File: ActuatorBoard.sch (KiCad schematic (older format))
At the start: 79 parts, among them J1 Screw_Terminal_01x02, J11 Screw_Terminal_01x02, J12 Screw_Terminal_01x02, J13 Screw_Terminal_01x04, J2 Screw_Terminal_01x02, J3 Screw_Terminal_01x02, J4 Screw_Terminal_01x02, J5 Screw_Terminal_01x02, J7 Screw_Terminal_01x02, J8 Screw_Terminal_01x02, J9 Screw_Terminal_01x02, K1 SANYOU_SRD_Form_B, K2 SANYOU_SRD_Form_B, K3 SANYOU_SRD_Form_B, P1 CONN_01X03, P10 CONN_01X03, P11 CONN_01X03, P12 CONN_01X03, P13 CONN_01X02, P14 SERVO_+, P15 SERVO_-, P16 CONN_01X03, P17 CONN_01X05, P18 CONN_01X08, P19 CONN_01X05, P2 CAN_Conn, P20 CONN_01X08, P21 STEPPER_VCC, P22 CONN_01X05, P23 CONN_01X04, P3 CONN_01X03, P4 CONN_01X03, P5 CONN_01X03, P7 CONN_01X03, P8 CONN_01X03, Q1 BS170, Q2 BS170, Q3 BS170, Q5 IRLR024, U1 MCP2551-I-SN, U2 AT90CAN128-16AU, U3 ULN2003, U4 L7805, Y1 Crystal, Y2 Crystal

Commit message: Added output files
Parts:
- added P6: CONN_01X06, Pin_Headers:Pin_Header_Straight_1x06, symbol CONN_01X06
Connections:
- net +5V: now also P6.1 (P1); no longer P22.1 (P1), P22.2 (P2), P22.3 (P3), P22.4 (P4), P22.5 (P5)
- net +5VD: now also P22.1 (P1), P22.2 (P2), P22.3 (P3), P22.4 (P4), P22.5 (P5)
- net DIRECTION: now also U2.10 ((~SS~)PB0); no longer U2.11 ((SCK)PB1)
- net GND: now also P6.6 (P6)
- net MINI_M2: now also U2.45 ((AD6)PA6); no longer U2.47 ((AD4)PA4)
- net MINI_M3: now also U2.44 ((AD7)PA7); no longer U2.46 ((AD5)PA5)
- net R1: now also U3.3 (I3), U3.4 (I4); no longer U3.1 (I1), U3.2 (I2)
- net R1_SIG: now also U3.13 (O4), U3.14 (O3); no longer U3.15 (O2), U3.16 (O1)
- net R2: now also U3.1 (I1), U3.2 (I2); no longer U3.3 (I3), U3.4 (I4)
- net R2_SIG: now also U3.15 (O2), U3.16 (O1); no longer U3.13 (O4), U3.14 (O3)
- net RX0: now also S1.4, P6.2 (P2); no longer S1.3
- net STEP: now also U2.11 ((SCK)PB1), P6.4 (P4); no longer U2.10 ((~SS~)PB0)
- net TX0: now also S1.3, P6.3 (P3); no longer S1.4
- net RESET: now reaches U2.20 (~RESET)
- net RESET: now also P6.5 (P5)
- net D2: now reaches R11.2
- net D2: now also U2.46 ((AD5)PA5); no longer U2.44 ((AD7)PA7)
- net D1: now reaches R12.2
- net D1: now also U2.47 ((AD4)PA4); no longer U2.45 ((AD6)PA6)
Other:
- moved on the sheet: D13, D14, R11, R12

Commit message: Changed the schematic to look more fancy (pdf update)
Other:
- note added: "3x MOSFET"
- note added: "3x Relay"
- note added: "ADC"
- note added: "AX connections & rx/tx switching"
- note added: "CAN pinout (MCP2551)"
- note added: "Darlington relay driver"
- note added: "Debug LED"
- note added: "Indicator for input\n"
- note added: "Input 12V with diode protection\n"
- note added: "Input 5V with mosfet protection\n\n"
- note added: "Output for I2C\n"
- note added: "PORTB pinout"
- note added: "PORTC pinout"
- note added: "Pinout for kinez servos"
- note added: "Programator pinout"
- note added: "Regulator for 5V logic\n"
- note added: "Stepper driver pinout (A4988)"
- moved on the sheet: A1, C1, C10, C2, C3, C4, C7, C8, C9, D10, D13, D14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

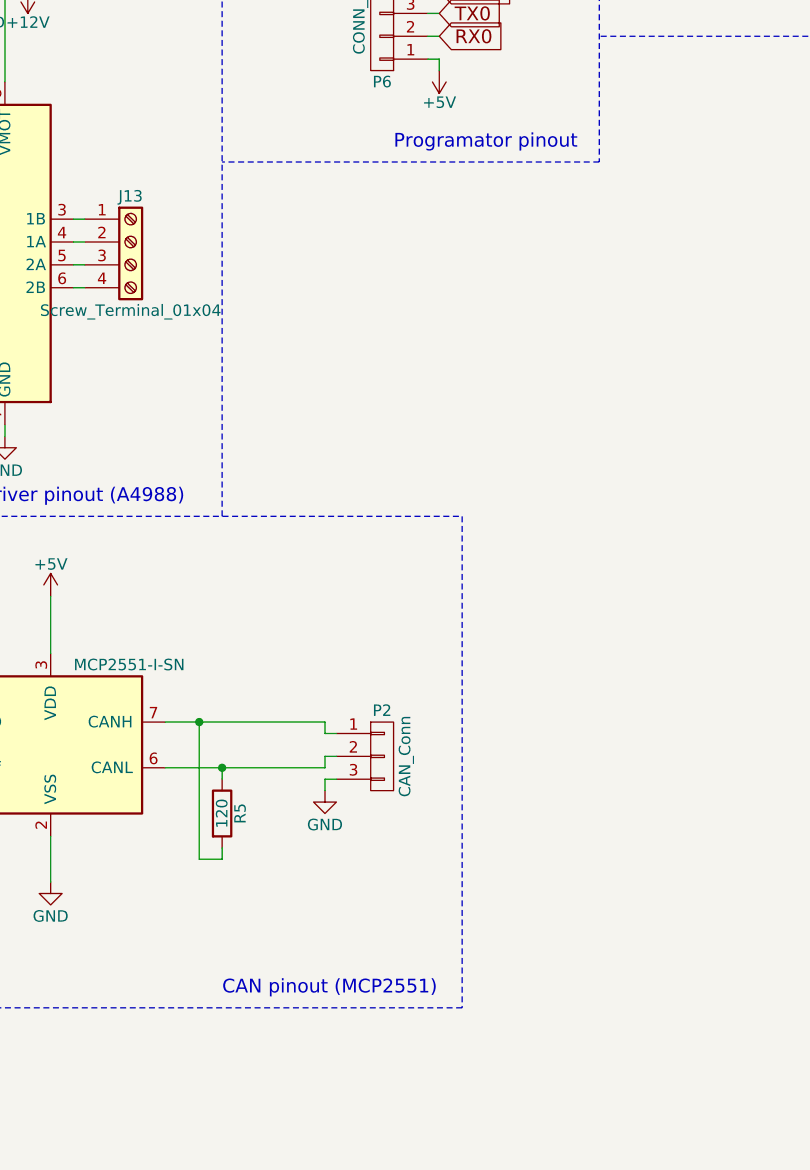
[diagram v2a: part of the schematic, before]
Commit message: Added new pdf, added tx rx debug pins
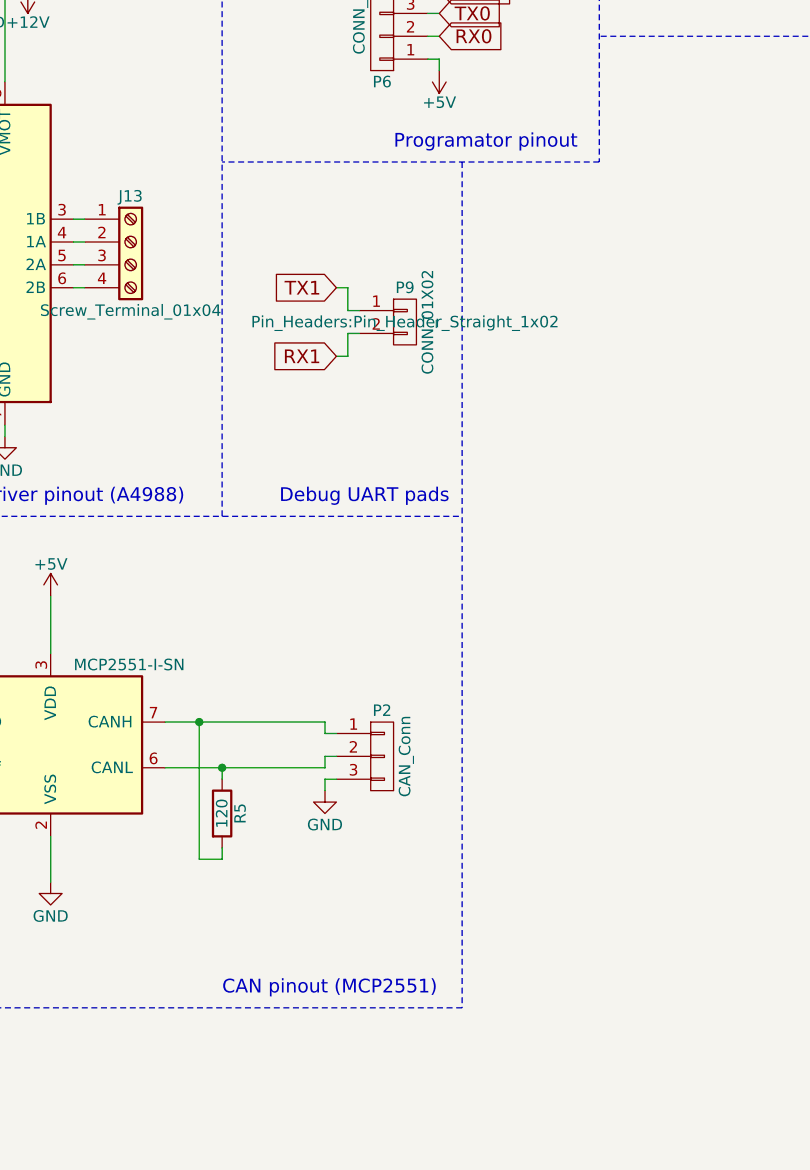
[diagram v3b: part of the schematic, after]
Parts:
- added P9: CONN_01X02, Pin_Headers:Pin_Header_Straight_1x02, symbol CONN_01X02
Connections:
- net RX1: now also P9.2 (P2)
- net TX1: now also P9.1 (P1)
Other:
- note added: "Debug UART pads\n"

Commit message: Added new wrl files, and did repairs
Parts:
- removed P9: CONN_01X02, Pin_Headers:Pin_Header_Straight_1x02, symbol CONN_01X02
- added P9: CONN_01X03, Pin_Headers:Pin_Header_Straight_1x03, symbol CONN_01X03
- C1, C2, C3, C4, C7, C8: value CP -> 100u
- C10, C9: value C -> 100n
- R10, R11, R12, R9: value 1K -> 330
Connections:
- net GND: now also J11.1 (Pin_1), J12.2 (Pin_2), P10.3 (P3), P11.3 (P3), P12.3 (P3), P15.1 (P1), P15.2 (P2), P15.3 (P3), P9.3 (P3)
- net RX1: now also P9.1 (P1)
- net STEP: now also U2.19 (PG4(TOSC1)); no longer P6.4 (P4), U2.11 ((SCK)PB1)
- net TX1: now also P9.2 (P2)
- new net SCK: P6.4 (P4), U2.11 ((SCK)PB1)

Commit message: Added new stuff
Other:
- note added: "Dual crystal (TH and SMD)"
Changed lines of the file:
@@
 $EndComp
 Connection ~ 9050 2900
+Text Notes 4800 4450 0    60   ~ 0
+Dual crystal (TH and SMD)
 $EndSCHEMATC

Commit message: 12V relays...
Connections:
- net +12V: now also K1.5, K2.5, K3.5, U3.9 (COM)
- net +5VD: no longer K1.5, K2.5, K3.5, U3.9 (COM)
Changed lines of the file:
@@
-$EndComp
-$Comp
-L VCOM #PWR67
-U 1 1 59F5ED05
-P 15350 1850
-F 0 "#PWR67" H 15350 1700 50  0001 C CNN
-F 1 "VCOM" H 15350 2000 50  0000 C CNN
-F 2 "" H 15350 1850 50  0001 C CNN
-F 3 "" H 15350 1850 50  0001 C CNN
-	1    15350 1850
-	1    0    0    -1
 $EndComp
 $Comp
@@
 Connection ~ 15550 1900
 Wire Wire Line
-	15350 1850 15350 1950
-Connection ~ 15350 1900
-Wire Wire Line
 	7500 8050 7500 8100
 Wire Wire Line
@@
 	7900 1000 7950 1000
 Wire Wire Line
-	15200 850  15200 750
+	15200 700  15200 850
 Connection ~ 15200 750
 Wire Wire Line
@@
 Text Notes 4800 4450 0    60   ~ 0
 Dual crystal (TH and SMD)
+$Comp
+L VCOM #PWR?
+U 1 1 5A0DF5D3
+P 15200 700
+F 0 "#PWR?" H 15200 550 50  0001 C CNN
+F 1 "VCOM" H 15200 850 50  0000 C CNN
+F 2 "" H 15200 700 50  0001 C CNN
+F 3 "" H 15200 700 50  0001 C CNN
+	1    15200 700
+	1    0    0    -1
+$EndComp
+Wire Wire Line
+	15350 1950 15350 1900
+Connection ~ 15350 1900
 $EndSCHEMATC

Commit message: Actuator board with modules
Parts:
- removed A1: Pololu_Breakout_A4988, A4988:A4988, symbol Pololu_Breakout_A4988
- removed C1, C2: 100u, Capacitors_ThroughHole:C_Radial_D7.5_L11.2_P2.5, symbol CP
- removed C10, C9: 100n, Capacitors_SMD:C_0805, symbol C
- removed C5, C6: C, Capacitors_SMD:C_0805, symbol C
- removed D1, D10, D4, D5, D8, D9: D, Diodes_ThroughHole:Diode_DO-41_SOD81_Vertical_KathodeUp, symbol D
- removed D13, D14: LED, LEDs:LED_0805, symbol LED
- removed J1, J11, J12, J4, J5, J7, J8, J9: Screw_Terminal_01x02, Terminal_Blocks:TerminalBlock_Pheonix_MKDS1.5-2pol, symbol Screw_Terminal_01x02
- removed J13: Screw_Terminal_01x04, Terminal_Blocks:TerminalBlock_Pheonix_PT-3.5mm_4pol, symbol Screw_Terminal_01x04
- removed K1, K2, K3: SANYOU_SRD_Form_B, Relays_ThroughHole:Relay_SANYOU_SRD_Series_Form_C, symbol SANYOU_SRD_Form_B
- removed P1, P10, P11, P12, P16, P3, P4, P5, P7, P8, P9: CONN_01X03, Pin_Headers:Pin_Header_Straight_1x03, symbol CONN_01X03
- removed P14: SERVO_+, Pin_Headers:Pin_Header_Straight_1x03, symbol CONN_01X03
- removed P15: SERVO_-, Pin_Headers:Pin_Header_Straight_1x03, symbol CONN_01X03
- removed P17, P19, P22: CONN_01X05, Pin_Headers:Pin_Header_Straight_1x05, symbol CONN_01X05
- removed P18, P20: CONN_01X08, Pin_Headers:Pin_Header_Straight_1x08, symbol CONN_01X08
- removed P2: CAN_Conn, Pin_Headers:Pin_Header_Straight_1x03, symbol CONN_01X03
- removed P21: STEPPER_VCC, Pin_Headers:Pin_Header_Straight_1x03, symbol CONN_01X03
- removed P23: CONN_01X04, Pin_Headers:Pin_Header_Straight_1x04, symbol CONN_01X04
- removed P6: CONN_01X06, Pin_Headers:Pin_Header_Straight_1x06, symbol CONN_01X06
- removed Q1, Q2, Q3: BS170, TO_SOT_Packages_THT:TO-92_Inline_Narrow_Oval, symbol BS170
- removed R1, R6, R7: R, Resistors_SMD:R_0805, symbol R
- removed R11, R12: 330, Resistors_SMD:R_0805, symbol R
- removed R2, R3: 1K, Resistors_SMD:R_0805, symbol R
- removed R4: 10K, Resistors_SMD:R_0805, symbol R
- removed R5: 120, Resistors_SMD:R_0805, symbol R
- removed S1: SW_DIP_x2, Buttons_Switches_ThroughHole:SW_DIP_x2_Piano, symbol SW_DIP_x2
- removed U1: MCP2551-I-SN, Housings_SOIC:SOIC-8_3.9x4.9mm_Pitch1.27mm, symbol MCP2551-I-SN
- removed U2: AT90CAN128-16AU, Housings_QFP:TQFP-64_14x14mm_Pitch0.8mm, symbol AT90CAN128-16AU
- removed U3: ULN2003, Housings_SOIC:SOIC-16_3.9x9.9mm_Pitch1.27mm, symbol ULN2003
- removed Y1: Crystal, Crystals:Crystal_HC49-SD_SMD, symbol Crystal
- removed Y2: Crystal, Crystals:Crystal_HC49-U_Vertical, symbol Crystal
- added A2: Arduino_Nano_v3.x, Modules:Arduino_Nano_WithMountingHoles, symbol Arduino_Nano_v3.x
- added C5, C6: 100u, Capacitors_THT:CP_Radial_D7.5mm_P2.50mm, symbol CP
- added J1, J4: CONN_02X04, Pin_Headers:Pin_Header_Straight_2x04_Pitch2.54mm, symbol CONN_02X04
- added J5: CONN_01X03, Pin_Headers:Pin_Header_Straight_1x03_Pitch2.54mm, symbol CONN_01X03
- added M1, M2, M3, M4, M5, M6: Aktuator_Module, Aktuator_Module:Aktuator_Module, symbol Aktuator_Module
- added MK1, MK2, MK3, MK4, MK5, MK6, MK7, MK8: Mounting_Hole, Mounting_Holes:MountingHole_3.2mm_M3_Pad_Via, symbol Mounting_Hole
- added P1: CONN_01X04, Pin_Headers:Pin_Header_Straight_1x04_Pitch2.54mm, symbol CONN_01X04
- C3, C4, C8: footprint Capacitors_SMD:c_elec_6.3x4.5 -> Capacitors_SMD:CP_Elec_6.3x4.5
- C7: footprint Capacitors_ThroughHole:C_Radial_D7.5_L11.2_P2.5 -> Capacitors_THT:CP_Radial_D7.5mm_P2.50mm
- J2, J3: footprint Terminal_Blocks:TerminalBlock_Pheonix_MKDS1.5-2pol -> Connectors_Terminal_Blocks:TerminalBlock_Pheonix_MKDS1.5-2pol
- P13: footprint Pin_Headers:Pin_Header_Straight_1x02 -> Pin_Headers:Pin_Header_Straight_1x02_Pitch2.54mm
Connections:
- net +12V: now also C5.1, J1.1 (P1), J1.2 (P2), J1.3 (P3), J1.4 (P4), J1.5 (P5), J1.6 (P6), J1.7 (P7), J1.8 (P8), M1.2 (12V), M2.2 (12V), M3.2 (12V), M4.2 (12V), M5.2 (12V), M6.2 (12V)
- net +5V: now also A2.27 (+5V)
- net +5VD: now also C6.1, J4.1 (P1), J4.2 (P2), J4.3 (P3), J4.4 (P4), J4.5 (P5), J4.6 (P6), J4.7 (P7), J4.8 (P8), M1.1 (5V), M2.1 (5V), M3.1 (5V), M4.1 (5V), M5.1 (5V), M6.1 (5V)
- net GND: now also A2.29 (GND), A2.4 (GND), C5.2, C6.2, J5.1 (P1), M1.4 (GND), M2.4 (GND), M3.4 (GND), M4.4 (GND), M5.4 (GND), M6.4 (GND), P1.1 (P1), P1.2 (P2), P1.3 (P3), P1.4 (P4)
- net PF0 renamed BAT_MAIN_ADC
- net BAT_MAIN_ADC: now also A2.25 (A6)
- net PF1 renamed BAT_ODO_ADC
- net BAT_ODO_ADC: now also A2.26 (A7)
- new net M_ADC_1: A2.19 (A0), M3.8 (S3)
- new net M_ADC_2: A2.20 (A1), M4.3 (SIG)
- new net M_ADC_3: A2.21 (A2), M4.6 (S1)
- new net M_ADC_4: A2.22 (A3), M4.7 (S2)
- new net M_ADC_5: A2.23 (A4), M5.3 (SIG)
- new net M_ADC_6: A2.24 (A5), M6.3 (SIG)
- new net RX: A2.2 (D0/RX), J5.3 (P3)
- new net SIG1: A2.5 (D2), M1.3 (SIG)
- new net SIG10: A2.14 (D11), M3.6 (S1)
- new net SIG11: A2.15 (D12), M3.7 (S2)
- new net SIG2: A2.6 (D3), M1.6 (S1)
- new net SIG3: A2.7 (D4), M1.7 (S2)
- new net SIG4: A2.8 (D5), M1.8 (S3)
- new net SIG5: A2.9 (D6), M2.3 (SIG)
- new net SIG6: A2.10 (D7), M2.6 (S1)
- new net SIG7: A2.11 (D8), M2.7 (S2)
- new net SIG8: A2.12 (D9), M2.8 (S3)
- new net SIG9: A2.13 (D10), M3.3 (SIG)
- new net TX: A2.1 (D1/TX), J5.2 (P2)
- no-connect marks 1 -> 15
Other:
- note added: "ADC for batteries"
- note added: "Arduino Nano"
- note added: "M1 - Module One\nSIG - D2 | S1 - D3 | S2 - D4 | S3 - D5 |\n\nM2 - Module Two\nSIG - D6 | S1 - D7 | S2 - D8 | S3 - D9 |\n\nM3 - Module Three\nSIG - D10 | S1 - D11 | S2 - D12 | S3 - A0 |\n\nM4 - Module Four\nSIG - A1 | S1 - A2 | S2 - A3 |\n\nM5 - Module Five\nSIG - A4\n\nM6 - Module Six\nSIG - A5"
- note added: "Modules\n"
- note added: "Mouting holes"
- note added: "PWM"
- note added: "Power pins"
- note added: "Power\nindicator\n\n"
- note added: "Serial"
- note removed: "3x MOSFET"
- note removed: "3x Relay"
- note removed: "ADC"
- note removed: "AX connections & rx/tx switching"
- note removed: "CAN pinout (MCP2551)"
- note removed: "Darlington relay driver"
- note removed: "Debug LED"
- note removed: "Debug UART pads\n"
- note removed: "Dual crystal (TH and SMD)"
- note removed: "Indicator for input\n"
- note removed: "Output for I2C\n"
- note removed: "PORTB pinout"
- note removed: "PORTC pinout"
- note removed: "Pinout for kinez servos"
- note removed: "Programator pinout"
- note removed: "Stepper driver pinout (A4988)"
- moved on the sheet: C3, C4, C7, C8, D2, D3, D7, J2, J3, P13, Q5, R10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
